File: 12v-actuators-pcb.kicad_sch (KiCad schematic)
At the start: 17 parts, among them J2 3.5mm WR-TBL, J3 690367280676, J5 65100516121, J7 RGBA_LEDs, J8 CAN, U1 MCP2551-I-SN

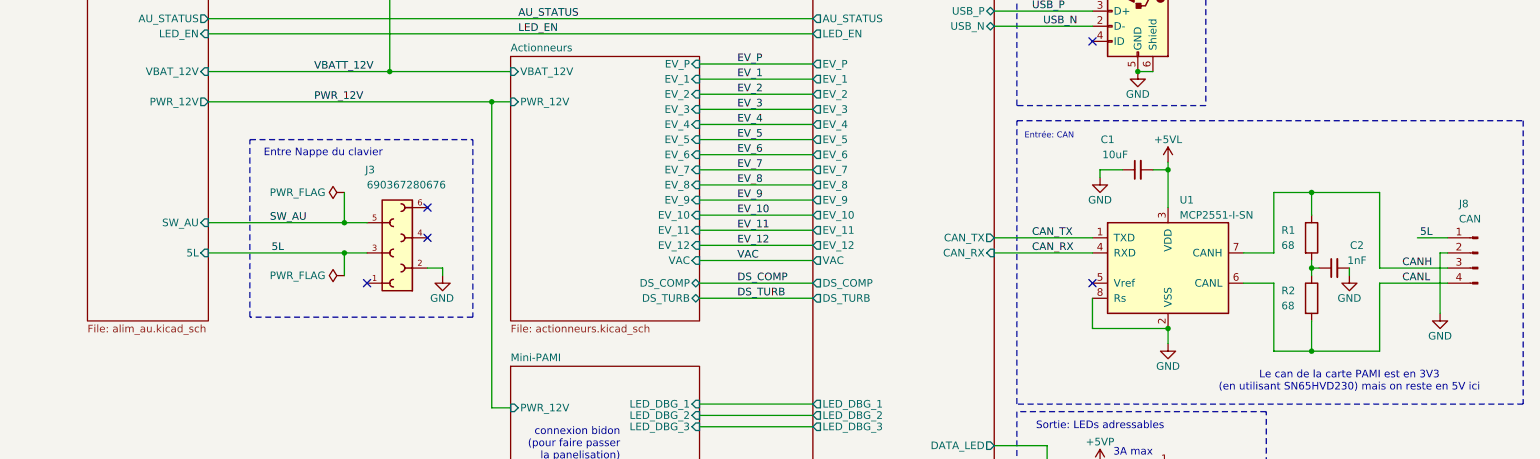
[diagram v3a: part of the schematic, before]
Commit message: mise à jour du schema après la coupe de belgique
- modification du circuit d'AU (SW_AU 24V->3.3V)
- modification du pinout de J3: ajout du CAN (suppression de J8) et du RST_EXT
- ajout d'un circuit de reset externe (configurable via 3-jumper)
- ajout d'un connecteur dédié pour un bouton reset externe
- ajout d'un debounce sur le switch reset
- mise à jour du routage et serigraphie
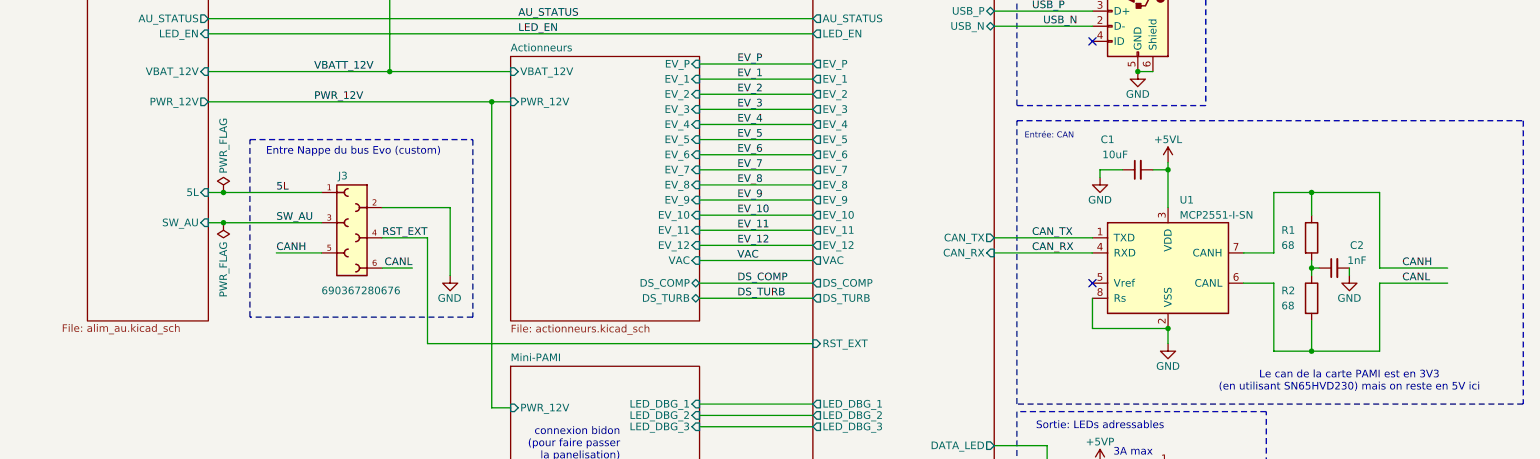
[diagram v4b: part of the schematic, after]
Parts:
- removed J8: CAN, Connector_PinHeader_2.54mm:PinHeader_1x04_P2.54mm_Vertical, symbol Connector:Conn_01x04_Pin
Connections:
- net 5L: now also J3.1; no longer J3.3
- net CANH: now also J3.5
- net CANL: now also J3.6
- net SW_AU: now also J3.3; no longer J3.5
- net RST_EXT: now reaches J3.4
- no-connect marks 5 -> 2
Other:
- sheet MCU et capteurs ports: added RST_EXT; removed none
- note added: "Entre Nappe du bus Evo (custom)"
- note removed: "Entre Nappe du clavier"
- moved on the sheet: J3
